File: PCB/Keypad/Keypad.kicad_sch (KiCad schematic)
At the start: 21 parts, among them J1 Keypad, J2 Shelly, U1 SP3485, U2 ESP32-PICO-MINI-02, U2 LMR16006YDDCR, U4 QR

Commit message: Tidy, new PSU and LED
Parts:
- removed C2: 100nF, RevK:C_0603_, symbol RevK:Hidden
- removed C3: 2.2uF, RevK:C_0805_, symbol RevK:Hidden
- removed C4: 10uF, RevK:C_0805_, symbol RevK:Hidden
- removed D1: LED_BARG, RevK:MHS190RGBCT, symbol Device:LED_BARG
- removed D2: Schottky, RevK:D_1206_, symbol RevK:Hidden
- removed L1: 6.8uH, RevK:L_4x4_, symbol RevK:Hidden
- removed R2: 680R, RevK:R_0603, symbol Device:R
- removed R3: 2K, RevK:R_0603, symbol Device:R
- removed R4: 220R, RevK:R_0603, symbol Device:R
- removed U2: LMR16006YDDCR, RevK:SOT-23-Thin-6-Reg, symbol RevK:LMR16006XDDCR
- added C10: 100nF, RevK:C_0603_, symbol RevK:Hidden
- added C8: 10uF 50V, RevK:C_0603_, symbol RevK:Hidden
- added C9: 10uF 6.3V, RevK:C_0603_, symbol RevK:Hidden
- added D2: RGB, RevK:LED-RGB-1.6x1.6, symbol Device:LED_RGBA
- added L2: 10uH, RevK:L_4x4_, symbol RevK:Hidden
- added R10: 39k2, RevK:R_0402_, symbol RevK:Hidden
- added R11: 1M, RevK:R_0402_, symbol RevK:Hidden
- added R12: 220R, RevK:R_0402, symbol Device:R
- added R9: 124k, RevK:R_0402_, symbol RevK:Hidden
- added U3: MD8942, RevK:SOT-23-6-MD8942, symbol RevK:MD89420-RegBlock
- C1, C5: footprint RevK:C_0603 -> RevK:C_0402
- R1: footprint RevK:R_0603 -> RevK:R_0402
- R5: value 100k 1% -> 680R; footprint RevK:R_0603 -> RevK:R_0402; LCSC Part # C14675 -> (none)
- R6: value 30k 1% -> 2K; footprint RevK:R_0603 -> RevK:R_0402; LCSC Part # C100001 -> (none)
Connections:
- net +12V: now also U3.5 (VIN)
- net +3V3: now also D2.4 (A), U3.8 (VOUT); no longer R5.1
- net B: now also R12.2
- net G: now also R6.2, U2.15 (IO25); no longer U2.16 (IO26)
- net GND: now also U3.2 (GND), U3.7 (GND); no longer R6.1
- net R: now also R5.2, U2.16 (IO26); no longer U2.15 (IO25)
- new net: D2.2 (GK), R6.1
- new net: D2.3 (BK), R12.1
- new net: D2.1 (RK), R5.1
- no-connect marks 18 -> 19

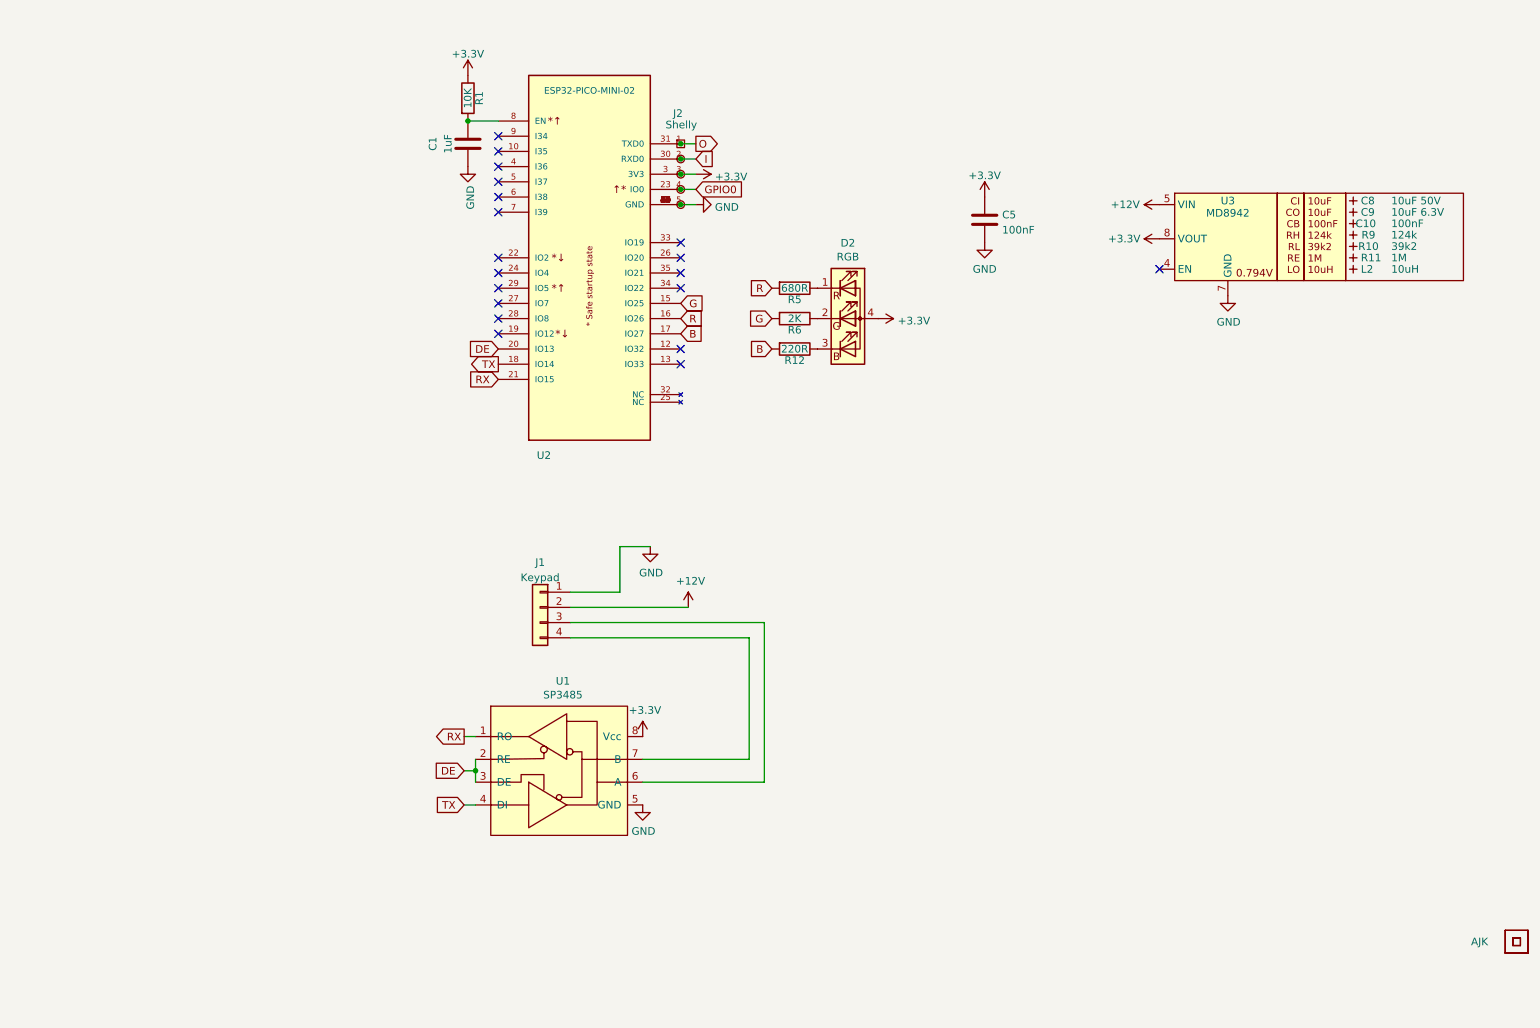
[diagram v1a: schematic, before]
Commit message: Re-designed for ESP32-S3
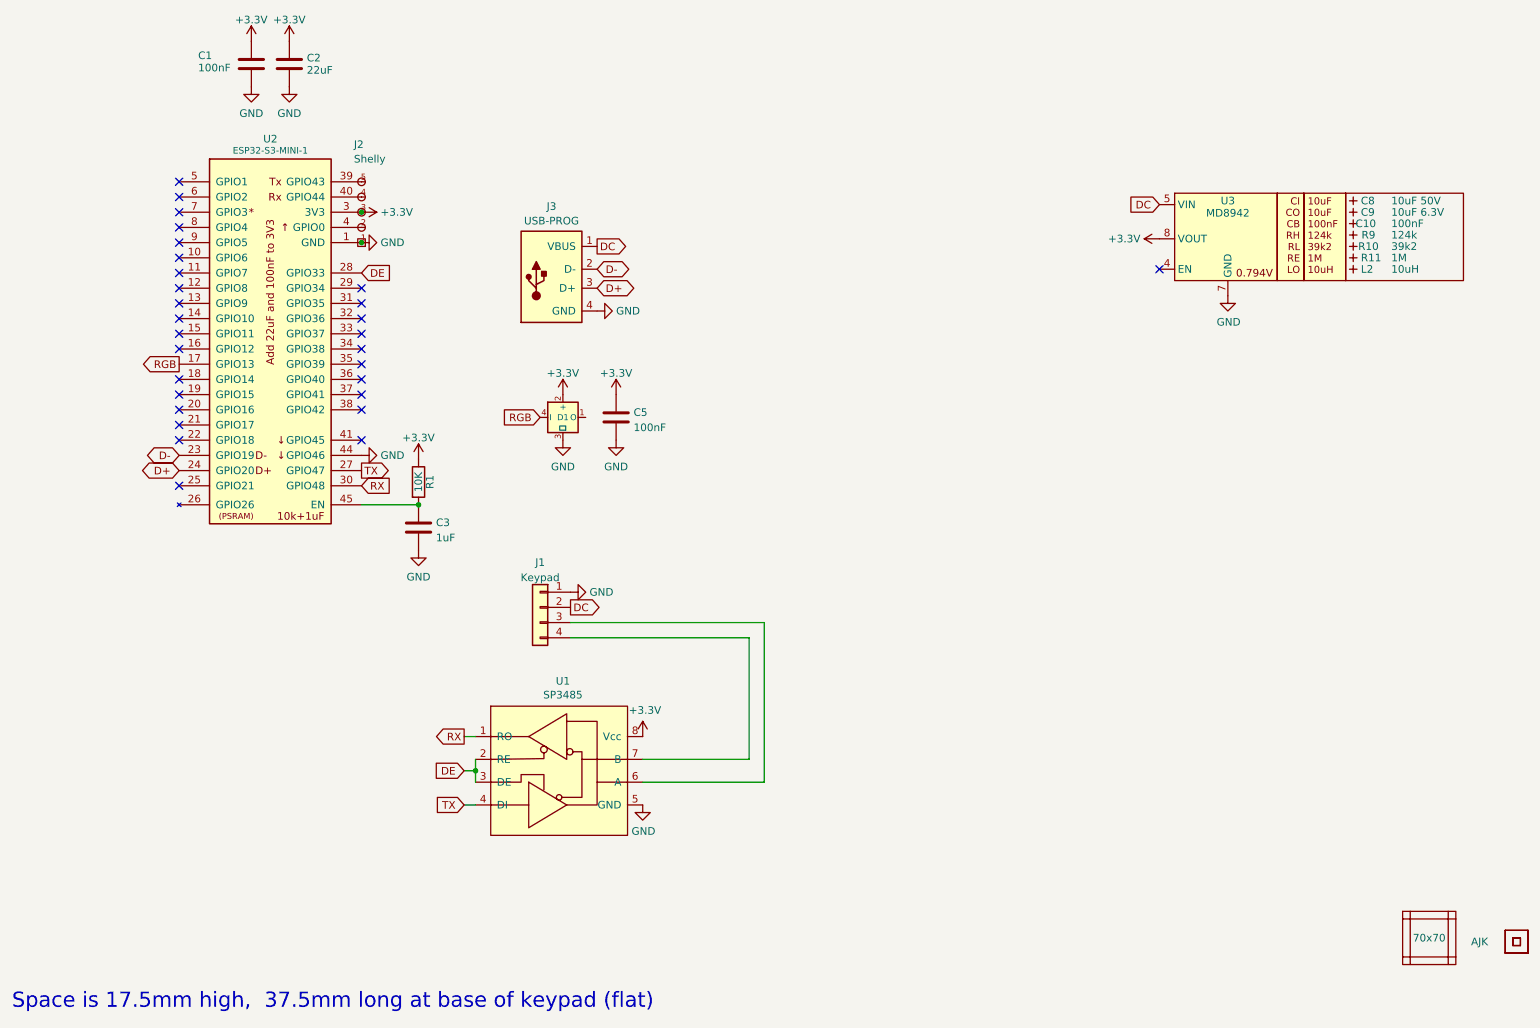
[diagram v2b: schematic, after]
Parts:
- removed D2: RGB, RevK:LED-RGB-1.6x1.6, symbol Device:LED_RGBA
- removed R12: 220R, RevK:R_0402, symbol Device:R
- removed R5: 680R, RevK:R_0402, symbol Device:R
- removed R6: 2K, RevK:R_0402, symbol Device:R
- removed U2: ESP32-PICO-MINI-02, RevK:ESP32-PICO-MINI-02, symbol RevK:ESP32-PICO-MINI-02
- added C2: 22uF, RevK:C_0603, symbol Device:C
- added C3: 1uF, RevK:C_0402, symbol Device:C
- added D1: XL-1010RGBC-WS2812B, RevK:SMD1010, symbol RevK:WS2812B-1mm
- added J3: USB-PROG, RevK:USB-PROG, symbol RevK:USB-PROG
- added PCB1: 70x70, RevK:PCB7070, symbol RevK:PCB
- added U2: ESP32-S3-MINI-1, RevK:ESP32-S3-MINI-1, symbol RevK:ESP32-S3-MINI-1-N4R2
- added V3, V4, V5, V6: ~, RevK:VCUT70N, symbol RevK:VCUT
- C1: value 1uF -> 100nF
- U1: footprint Package_SO:SO-8_3.9x4.9mm_P1.27mm -> RevK:SO-8_3.9x4.9mm_P1.27mm
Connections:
- net O is gone; now on net GND: J2.1 (GND)
- net +3V3: now also C1.1, C2.1, D1.2 (+), U2.3 (3V3)
- net DE: now also U2.28 (GPIO33)
- net GND: now also C1.2, C2.2, C3.2, D1.3 (⏚), J3.4 (GND), U2.1 (GND), U2.2 (GND), U2.42 (GND), U2.43 (GND), U2.44 (GPIO46), U2.46 (GND), U2.47 (GND), U2.48 (GND), U2.49 (GND), U2.50 (GND), U2.51 (GND), U2.52 (GND), U2.53 (GND), U2.54 (GND), U2.55 (GND), U2.56 (GND), U2.57 (GND), U2.58 (GND), U2.59 (GND), U2.60 (GND), U2.61 (GND), U2.62 (GND), U2.63 (GND), U2.64 (GND), U2.65 (GND); no longer C1.1, J2.5 (Tx)
- net RX: now also U2.30 (GPIO48)
- net TX: now also U2.27 (GPIO47)
- net at R1.2: now also C3.1, U2.45 (EN); no longer C1.2
- net +12V renamed DC
- net DC: now also J3.1 (VBUS)
- net GPIO0: no longer names the net of J2.4 (Rx)
- net GPIO0: now also U2.40 (GPIO44)
- net I: no longer names the net of J2.2 (0)
- net I: now also U2.4 (GPIO0)
- new net: J2.5 (Tx), U2.39 (GPIO43)
- new net D+: J3.3 (D+), U2.24 (GPIO20)
- new net D-: J3.2 (D-), U2.23 (GPIO19)
- new net RGB: D1.4 (I), U2.17 (GPIO13)
- no-connect marks 19 -> 29
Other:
- note added: "Space is 17.5mm high, 37.5mm long at base of keypad (flat)"
- moved on the sheet: C5

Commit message: Library update
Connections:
- net RGB renamed LED
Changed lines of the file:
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@@
     )
   )
-  (global_label "RGB" (shape output) (at 50.8 76.2 180) (fields_autoplaced)
+  (global_label "LED" (shape output) (at 50.8 76.2 180) (fields_autoplaced)
     (effects (font (size 1.27 1.27)) (justify right))
-    (property "Intersheetrefs" "${INTERSHEET_REFS}" (at 44.659 76.2 0)
+    (property "Intersheetrefs" "${INTERSHEET_REFS}" (at 45.0219 76.2 0)
       (effects (font (size 1.27 1.27)) (justify right) hide)
     )
@@
     )
   )
-  (global_label "RGB" (shape input) (at 111.125 85.09 180) (fields_autoplaced)
+  (global_label "LED" (shape input) (at 111.125 85.09 180) (fields_autoplaced)
     (effects (font (size 1.27 1.27)) (justify right))
-    (property "Intersheetrefs" "${INTERSHEET_REFS}" (at 104.984 85.09 0)
+    (property "Intersheetrefs" "${INTERSHEET_REFS}" (at 105.3469 85.09 0)
       (effects (font (size 1.27 1.27)) (justify right) hide)
     )
@@
     )
   )
-  (symbol (lib_id "RevK:WS2812B-1mm") (at 114.935 85.09 0) (unit 1)
-    (in_bom yes) (on_board yes) (dnp no) (fields_autoplaced)
+  (symbol (lib_id "RevK:WS2812B-1mm") (at 114.935 85.09 0) (mirror x) (unit 1)
+    (in_bom yes) (on_board yes) (dnp no)
     (property "Reference" "D1" (at 114.935 85.09 0) (do_not_autoplace)
       (effects (font (size 1 1)))
     )
-    (property "Value" "XL-1010RGBC-WS2812B" (at 116.205 90.805 0)
+    (property "Value" "XL-1010RGBC-WS2812B" (at 116.205 79.375 0)
       (effects (font (size 1 1)) (justify left top) hide)
     )
-    (property "Footprint" "RevK:SMD1010" (at 116.205 92.71 0)
+    (property "Footprint" "RevK:SMD1010" (at 116.205 77.47 0)
       (effects (font (size 1 1)) (justify left top) hide)
     )
-    (property "Datasheet" "https://datasheet.lcsc.com/lcsc/2301111010_XINGLIGHT-XL-1010RGBC-WS2812B_C5349953.pdf" (at 116.205 94.615 0)
+    (property "Datasheet" "https://datasheet.lcsc.com/lcsc/2301111010_XINGLIGHT-XL-1010RGBC-WS2812B_C5349953.pdf" (at 116.205 75.565 0)
       (effects (font (size 1 1)) (justify left top) hide)
     )
-    (property "LCSC Part #" "C5349953" (at 116.205 96.52 0)
+    (property "LCSC Part #" "C5349953" (at 116.205 73.66 0)
       (effects (font (size 1 1)) (justify left top) hide)
     )

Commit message: Library update
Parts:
- C8: value 10uF 50V -> 10uF 35V; LCSC Part # C1591 -> C194427
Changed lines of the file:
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@@
       (effects (font (size 1.27 1.27)) (justify left))
     )
-    (property "Value" "10uF 50V" (at 253.365 48.895 0)
+    (property "Value" "10uF 35V" (at 253.365 48.895 0)
       (effects (font (size 1.27 1.27)) (justify left))
     )
@@
       (effects (font (size 1.27 1.27)) hide)
     )
-    (property "LCSC Part #" "C1591" (at 247.015 48.895 0)
+    (property "LCSC Part #" "C194427" (at 247.015 48.895 0)
       (effects (font (size 1.27 1.27)) hide)
     )

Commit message: Library update
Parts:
- removed J2: Shelly, RevK:Shelly, symbol RevK:Shelly
- removed J3: USB-PROG, RevK:USB-PROG, symbol RevK:USB-PROG
- added J4: TC2030-USB-NL-DS, RevK:Tag-Connect_TC2030-IDC-NL_2x03_P1.27mm_Vertical, symbol RevK:TC2030-USB-NL
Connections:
- net +3V3: now also U2.19 (GPIO15)
- net D+: now also J4.4 (D+)
- net D-: now also J4.3 (D-)
- net DC: now also J4.1 (VBUS), J4.2 (VBUS)
- net GND: now also J4.5 (GND), J4.6 (GND)
- no-connect marks 29 -> 32
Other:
- moved on the sheet: C10, C8, C9, L2, R10, R11, R9, U3

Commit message: PCB Update
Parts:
- C6: renamed from C8; LCSC Part # C194427 -> (none); MPN (none) -> C194427
- C7: renamed from C9; LCSC Part # C1691 -> (none); MPN (none) -> C1691
- D1: LCSC Part # C5349953 -> (none); MPN (none) -> C5349953
- U1: JLCPCB Rotation Offset -90 -> (none)
- U3: renamed from U2; LCSC Part # C3013941 -> (none); MPN (none) -> C3013941
- U5: renamed from U3; LCSC Part # C2684786 -> (none); MPN (none) -> C2684786
- renumbered C1 to C2, C2 to C3, C3 to C4, C10 to C8, R9 to R5, R10 to R6, R1 to R7, R11 to R9, V3 to V1, V5 to V3, V6 to V4, V4 to V6
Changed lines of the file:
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@@
 (kicad_sch
-	(version 20231120)
+	(version 20241209)
 	(generator "eeschema")
-	(generator_version "8.0")
+	(generator_version "9.0")
 	(paper "A4")
 	(title_block
@@
 		(comment 2 "www.me.uk")
 	)
+	(text "Space is 17.5mm high,  37.5mm long at base of keypad (flat)"
+		(exclude_from_sim no)
+		(at 22.86 184.15 0)
+		(effects
+			(font
+				(size 2.54 2.54)
+			)
+			(justify left bottom)
+		)
+	)
 	(junction
 		(at 100.33 144.145)
@@
 		)
 	)
-	(text "Space is 17.5mm high,  37.5mm long at base of keypad (flat)"
-		(exclude_from_sim no)
-		(at 22.86 184.15 0)
-		(effects
-			(font
-				(size 2.54 2.54)
-			)
-			(justify left bottom)
-		)
-	)
 	(global_label "DC"
 		(shape output)
@@
 			)
 		)
-		(property "JLCPCB Rotation Offset" "-90"
-			(at 114.3 152.4 0)
-			(effects
-				(font
-					(size 1.27 1.27)
-				)
-				(hide yes)
-			)
-		)
 		(pin "1"
 		)
@@
 		(dnp no)
 		(fields_autoplaced yes)
-		(property "Reference" "V6"
+		(property "Reference" "V4"
 			(at 261.62 172.085 0)
 			(effects
@@
 		(dnp no)
 		(fields_autoplaced yes)
-		(property "Reference" "#PWR0105"
+		(property "Reference" "#PWR029"
 			(at 90.805 113.665 0)
 			(effects
@@
 		(dnp no)
 		(fields_autoplaced yes)
-		(property "Reference" "C2"
+		(property "Reference" "C3"
 			(at 72.136 25.011 0)
 			(effects
@@
 		(on_board yes)
 		(dnp no)
-		(property "Reference" "C9"
+		(property "Reference" "C7"
 			(at 189.23 51.435 0)
 			(effects
@@
 			)
 		)
-		(property "LCSC Part #" "C1691"
+		(property "MPN" "C1691"
 			(at 187.96 51.435 0)
 			(effects
@@
 		(dnp no)
 		(fields_autoplaced yes)
-		(property "Reference" "V5"
+		(property "Reference" "V3"
 			(at 255.27 172.085 0)
 			(effects
@@
 		(dnp no)
 		(fields_autoplaced yes)
-		(property "Reference" "V4"
+		(property "Reference" "V6"
 			(at 259.715 173.99 0)
 			(effects
@@
 		(dnp no)
 		(fields_autoplaced yes)
-		(property "Reference" "#PWR011"
+		(property "Reference" "#PWR015"
 			(at 62.865 36.195 0)
 			(effects
@@
 		(on_board yes)
 		(dnp no)
-		(property "Reference" "C10"
+		(property "Reference" "C8"
 			(at 191.77 53.34 90)
 			(effects
@@
 		(on_board yes)
 		(dnp no)
-		(property "Reference" "#PWR01"
+		(property "Reference" "#PWR07"
 			(at 87.63 91.44 0)
 			(effects
@@
 		(on_board yes)
 		(dnp no)
-		(property "Reference" "R11"
+		(property "Reference" "R9"
 			(at 189.23 59.055 0)
 			(effects
@@
 		(dnp no)
 		(fields_autoplaced yes)
-		(property "Reference" "#PWR0106"
+		(property "Reference" "#PWR028"
 			(at 90.805 95.885 0)
 			(effects
@@
 		(dnp no)
 		(fields_autoplaced yes)
-		(property "Reference" "#PWR01"
+		(property "Reference" "#PWR011"
 			(at 159.385 55.88 0)
 			(effects
@@
 		(on_board yes)
 		(dnp no)
-		(property "Reference" "#PWR02"
+		(property "Reference" "#PWR012"
 			(at 167.005 71.755 0)
 			(effects
@@
 		(dnp no)
 		(fields_autoplaced yes)
-		(property "Reference" "V3"
+		(property "Reference" "V1"
 			(at 259.715 167.64 0)
 			(effects
@@
 		(dnp no)
 		(fields_autoplaced yes)
-		(property "Reference" "#PWR03"
+		(property "Reference" "#PWR019"
 			(at 77.47 50.8 0)
 			(effects
@@
 		(dnp no)
 		(fields_autoplaced yes)
-		(property "Reference" "#PWR012"
+		(property "Reference" "#PWR014"
 			(at 69.215 26.035 0)
 			(effects
@@
 		(dnp no)
 		(fields_autoplaced yes)
-		(property "Reference" "#PWR08"
+		(property "Reference" "#PWR013"
 			(at 62.865 26.035 0)
 			(effects
@@
 		(on_board yes)
 		(dnp no)
-		(property "Reference" "R1"
+		(property "Reference" "R7"
 			(at 92.71 95.885 90)
 			(effects
@@
 		(dnp no)
 		(fields_autoplaced yes)
-		(property "Reference" "#PWR0105"
+		(property "Reference" "#PWR03"
 			(at 122.555 114.3 0)
 			(effects
@@
 		(on_board yes)
 		(dnp no)
-		(property "Reference" "R9"
+		(property "Reference" "R5"
 			(at 190.5 55.245 0)
 			(effects
@@
 		(dnp no)
 		(fields_autoplaced yes)
-		(property "Reference" "U2"
+		(property "Reference" "U3"
 			(at 66.04 38.5532 0)
 			(effects
@@
 			)
 		)
-		(property "LCSC Part #" "C3013941"
+		(property "MPN" "C3013941"
 			(at 66.04 104.775 0)
 			(effects
@@
 		(on_board yes)
 		(dnp no)
-		(property "Reference" "R10"
+		(property "Reference" "R6"
 			(at 190.5 57.15 90)
 			(effects
@@
 		(dnp no)
 		(fields_autoplaced yes)
-		(property "Reference" "#PWR013"
+		(property "Reference" "#PWR018"
 			(at 69.215 36.195 0)
 			(effects
@@
 		(dnp no)
 		(fields_autoplaced yes)
-		(property "Reference" "C3"
+		(property "Reference" "C4"
 			(at 93.726 102.6703 0)
 			(effects
@@
 		(on_board yes)
 		(dnp no)
-		(property "Reference" "U3"
+		(property "Reference" "U5"
 			(at 167.005 49.53 0)
 			(effects
@@
 			)
 		)
-		(property "LCSC Part #" "C2684786"
+		(property "MPN" "C2684786"
 			(at 167.005 82.55 0)
 			(effects
@@
 		(dnp no)
 		(fields_autoplaced yes)
-		(property "Reference" "#PWR0105"
+		(property "Reference" "#PWR04"
 			(at 114.935 95.25 0)
 			(effects
@@
 		(dnp no)
 		(fields_autoplaced yes)
-		(property "Reference" "#PWR0106"
+		(property "Reference" "#PWR06"
 			(at 114.935 85.09 0)
 			(effects
@@
 		(dnp no)
 		(fields_autoplaced yes)
-		(property "Reference" "#PWR01"
+		(property "Reference" "#PWR020"
 			(at 87.63 55.88 0)
 			(effects
@@
 		(on_board yes)
 		(dnp no)
-		(property "Reference" "C1"
+		(property "Reference" "C2"
 			(at 53.975 24.622 0)
 			(effects
@@
 			)
 		)
-		(property "LCSC Part #" "C5349953"
+		(property "MPN" "C5349953"
 			(at 116.205 73.66 0)
 			(effects
@@
 		(on_board yes)
 		(dnp no)
-		(property "Reference" "C8"
+		(property "Reference" "C6"
 			(at 189.23 49.53 0)
 			(effects
@@
 			)
 		)
-		(property "LCSC Part #" "C194427"
+		(property "MPN" "C194427"
 			(at 187.96 49.53 0)
 			(effects
@@
 		)
 	)
+	(embedded_fonts no)
 )
